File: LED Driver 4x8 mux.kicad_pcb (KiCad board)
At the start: 2 copper layers, 117 x 127.1 mm, 34 parts, among them J1 Barrel_Jack_Switch, J2 Conn_01x04_Female, J3 8P8C_Shielded_x4, M1 Fan_4pin, M2 Fan_4pin, M3 Fan_4pin, M4 Fan_4pin, Q1 SUM70060E, Q2 SUM70060E, Q3 SUM70060E, Q4 SUM70060E, Q5 DMN32D2LDF-7, Q6 DMN32D2LDF-7, U1 MIC4468ZWM-TR, U2 DC DC Converter

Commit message: update PCB
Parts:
- removed D1, D2, D3, D4: TVS_Diode, Custom Footprints:DO-214AA
- removed HS1, HS2: HS-PCB, Custom Footprints:Heatsink_910-40-2-23-2-B-0
- removed J2: Conn_01x04_Female, Custom Footprints:DC_DC_converter-3S4A_1218S1UP
- removed JP1, JP2, JP3, JP4, JP5: Quick Connect, Custom Footprints:4928TR-power
- removed M1, M2, M3, M4: Fan_4pin, Custom Footprints:4-pin_fan_SMD
- removed Q5, Q6: DMN32D2LDF-7, Package_TO_SOT_SMD:SOT-353_SC-70-5
- added C1: 22µF, Capacitor_SMD:C_1206_3216Metric, F.Cu at (227.6, 49.0)
- added C2: 2.2uF, Custom Footprints:0508_Capacitor, F.Cu at (243.7, 37.6)
- added C3: 22µF, Capacitor_SMD:C_1206_3216Metric, F.Cu at (236.1, 44.0)
- added C5: 2.2uF, Custom Footprints:0508_Capacitor, F.Cu at (252.3, 31.0)
- added U3: MIC4467YWM-TR, Custom Footprints:TC4468EOE, F.Cu at (218.4, 47.0)
- Q1, Q2, Q3, Q4: value SUM70060E -> IRF9358TRPBF-2x_p-channel; footprint Package_TO_SOT_SMD:TO-263-2 -> Custom Footprints:IRF9358TRPBF-2x_p-channel
- U1: value MIC4468ZWM-TR -> SN74LV138AT_D_16; footprint Custom Footprints:MIC4468ZWM-TR -> Custom Footprints:SN74LV138ATD
- U2: value DC DC Converter -> MIC4467YWM-TR; footprint Custom Footprints:Ref_only -> Custom Footprints:TC4468EOE
- moved U1 156.5 mm to (229.1, 34.8), turned to 0 degrees
- moved Q1 142.2 mm to (237.6, 32.3), turned to 0 degrees
- moved Q2 114.6 mm to (229.1, 44.0), turned to 0 degrees
- moved Q3 110.6 mm to (237.6, 39.0), turned to 0 degrees
- moved Q4 108.2 mm to (246.2, 32.3), turned to 0 degrees
- moved U2 42.1 mm to (218.4, 35.0)
- renumbered C1 to C4
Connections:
- C4 pad 2: /18V -> /+18V
- J1 pad 1: /12V -> /+18V
- J3 pad 1: Net-(J3-Pad1) -> /LED5+
- J3 pad 17: /CH1 -> /LED+
- J3 pad 18: GND -> /LED-
- J3 pad 19: /CH2 -> /LED+
- J3 pad 2: Net-(J3-Pad2) -> /LED-
- J3 pad 20: GND -> /LED-
- J3 pad 21: /CH3 -> /LED+
- J3 pad 22: GND -> /LED-
- J3 pad 23: /CH4 -> /LED+
- J3 pad 24: GND -> /LED-
- J3 pad 25: /Thermistor -> /LED1+
- J3 pad 26: /Therm1 -> /LED-
- J3 pad 27: /Thermistor -> /LED2+
- J3 pad 28: /Therm2 -> /LED-
- J3 pad 29: /Thermistor -> /LED3+
- J3 pad 3: /OUT2 -> /LED6+
- J3 pad 30: /Therm3 -> /LED-
- J3 pad 31: /Thermistor -> /LED4+
- J3 pad 32: /Therm4 -> /LED-
- J3 pad 4: GND -> /LED-
- J3 pad 5: /OUT3 -> /LED7+
- J3 pad 6: GND -> /LED-
- J3 pad 7: Net-(J3-Pad7) -> /LED8+
- J3 pad 8: Net-(J3-Pad8) -> /LED-
- J3 pad 9: /Fan_PWM -> /OUT1
- Q1 pad 1: /Gate4 -> /LED+
- Q1 pad 2: /LED4- -> /Gate1
- Q1 pad 3: /LED- -> /LED+
- Q2 pad 1: /Gate3 -> /LED+
- Q2 pad 2: /LED3- -> /Gate3
- Q2 pad 3: /LED- -> /LED+
- Q3 pad 1: /Gate2 -> /LED+
- Q3 pad 2: /LED2- -> /Gate5
- Q3 pad 3: /LED- -> /LED+
- Q4 pad 1: /Gate1 -> /LED+
- Q4 pad 2: /LED1- -> /Gate7
- Q4 pad 3: /LED- -> /LED+
- U1 pad 1: /CH4 -> /OUT1
- U1 pad 10: /CH1 -> /IN6
- U1 pad 11: /Gate1 -> /IN5
- U1 pad 12: /Gate2 -> /IN4
- U1 pad 13: /Gate3 -> /IN3
- U1 pad 14: /Gate4 -> /IN2
- U1 pad 15: /18V -> /IN1
- U1 pad 16: /18V -> /+5V
- U1 pad 2: /CH4 -> /OUT2
- U1 pad 3: /CH3 -> /OUT3
- U1 pad 4: /CH3 -> GND
- U1 pad 5: /CH2 -> GND
- U1 pad 6: /CH2 -> /+5V
- U1 pad 9: /CH1 -> /IN7
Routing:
- net /LED-: track 41.9 -> 244.9 mm, vias 0 -> 2
- net /OUT1: track 0.00 -> 198.6 mm
- net /Fan_PWM: track 198.6 -> 0.00 mm
- net GND: track 641.9 -> 498.1 mm, vias 109 -> 107
- net /LED+: track 59.0 -> 199.1 mm
- net /12V: track 134.8 -> 0.00 mm
- net /+18V: track 0.00 -> 134.8 mm
- net /Therm2: track 59.3 -> 0.00 mm
- net /CH1: track 56.8 -> 0.00 mm
- net /CH2: track 43.6 -> 0.00 mm
- net /CH3: track 39.8 -> 0.00 mm
- added copper zone on F.Cu, net /+18V
- removed copper zone on F.Cu, net /18V

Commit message: PCB draft finished
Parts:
- added PS1: PXO7805-500-M-TR, Custom Footprints:18V_to_5V_PXO7805-500-M-TR, F.Cu at (91.8, 131.8)
- Q1, Q2, Q3, Q4: value IRF9358TRPBF-2x_p-channel -> SO8_IRF9358TRPBF_INF
- moved C3 163.9 mm to (99.8, 135.0), turned to 90 degrees
- moved C2 162.3 mm to (107.7, 126.2)
- moved C1 157.8 mm to (88.7, 123.8)
- moved U1 156.3 mm to (107.3, 132.9)
- moved Q4 151.4 mm to (136.1, 136.2)
- moved C5 149.4 mm to (128.9, 115.2), turned to 270 degrees
- moved Q3 136.2 mm to (136.1, 129.8)
- moved Q1 132.2 mm to (136.1, 117.0)
- moved U3 129.6 mm to (121.4, 132.9)
- moved U2 128.9 mm to (121.7, 120.2)
- moved Q2 122.3 mm to (136.1, 123.4)
- moved H1 51.4 mm to (86.8, 97.4)
- moved H2 51.4 mm to (188.4, 97.4)
- moved LOGO1 44.6 mm to (168.4, 103.4), turned to 0 degrees
- moved LOGO3 41.1 mm to (169.6, 100.3), turned to 0 degrees
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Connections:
- J3 pad 1: /LED5+ -> /LED1+
- J3 pad 10: GND -> /LED-
- J3 pad 11: /OUT2 -> /LED6+
- J3 pad 12: GND -> /LED-
- J3 pad 13: /OUT3 -> /LED7+
- J3 pad 14: GND -> /LED-
- J3 pad 15: /Thermistor -> /LED8+
- J3 pad 16: GND -> /LED-
- J3 pad 25: /LED1+ -> /OUT1
- J3 pad 26: /LED- -> GND
- J3 pad 27: /LED2+ -> /OUT2
- J3 pad 28: /LED- -> GND
- J3 pad 29: /LED3+ -> /OUT3
- J3 pad 3: /LED6+ -> /LED2+
- J3 pad 30: /LED- -> GND
- J3 pad 31: /LED4+ -> /Thermistor
- J3 pad 32: /LED- -> GND
- J3 pad 5: /LED7+ -> /LED3+
- J3 pad 7: /LED8+ -> /LED4+
- J3 pad 9: /OUT1 -> /LED5+
- U1 pad 7: GND -> /IN8
- U3 pad 10: Net-(U3-Pad10) -> /IN8
- U3 pad 9: Net-(U3-Pad10) -> /IN8
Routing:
- net /LED+: track 199.1 -> 45.2 mm, vias 118 -> 0
- net /OUT1: track 198.6 -> 58.7 mm
- net GND: track 498.1 -> 382.6 mm, vias 107 -> 206
- net /Gate1: track 108.7 -> 8.01 mm
- net /Gate2: track 86.3 -> 7.49 mm
- net /LED2-: track 70.5 -> 0.00 mm
- net /LED3-: track 70.3 -> 0.00 mm
- net /LED4-: track 70.3 -> 0.00 mm
- net /Therm1: track 59.5 -> 0.00 mm
- net /Therm3: track 52.5 -> 0.00 mm
- net /Therm4: track 51.9 -> 0.00 mm
- net /Gate3: track 59.3 -> 8.21 mm
- net /LED1+: track 0.00 -> 48.1 mm
- net /LED2+: track 0.00 -> 44.4 mm
- net /LED-: track 244.9 -> 288.4 mm, vias 2 -> 0
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- removed copper zone on F.Cu, net /+18V
- removed copper zone on B.Cu, net /LED+
- removed copper zone on F.Cu, net /LED1-
- removed copper zone on F.Cu, net /LED2-
- removed copper zone on F.Cu, net /LED3-
- removed copper zone on F.Cu, net /LED4-
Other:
- board size 117 x 127.1 mm -> 117 x 72.4 mm
- board text added: "12-18V DC"
- board text added: "Designed by: Benjamin E. Smith Funded by: NIH P30EY003176 https://github.com/Llamero/High_speed_1x8_LED_mux"
- board text added: "High Speed 1:8 LED Mux"
- board text added: "LED Input 4 3 2 1"
- board text added: "LED Output 4 3 2 1"
- board text added: "LED Output 8 7 6 5"
- board text added: "Therm OUT3 OUT2 OUT1"
- board text removed: "*"
- board text removed: "+"
- board text removed: "+ - LED 1"
- board text removed: "+ - LED 2"
- board text removed: "+ - LED 3"
- board text removed: "+ - LED 4"
- board text removed: "-"
- board text removed: "12V"
- board text removed: "12V DC"
- board text removed: "18V"
- board text removed: "Channel Select 4 3 2 1"
- board text removed: "Designed by: Benjamin E. Smith Funded by: NIH P30EY003176 https://github.com/Llamero/High-current-4x1-LED-mux"
- board text removed: "GND"
- board text removed: "High Current 4:1 Mux"
- board text removed: "LED Fan"
- board text removed: "LED Input"
- board text removed: "LED Thermistor 4 3 2 1"
- board text removed: "N/C OUT3 OUT2 N/C"
- board text removed: "Therm OUT3 OUT2 Fan PWM"

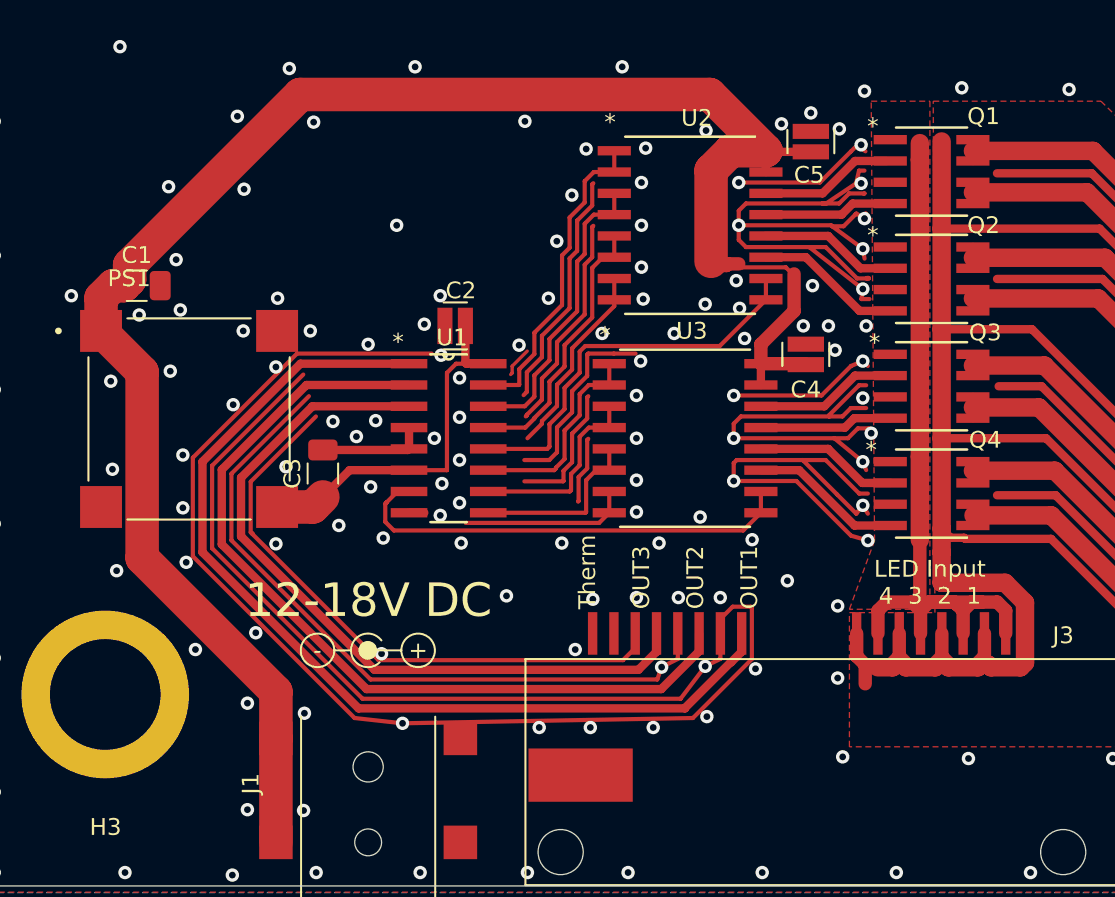
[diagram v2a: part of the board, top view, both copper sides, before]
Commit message: Add thermistor breakout
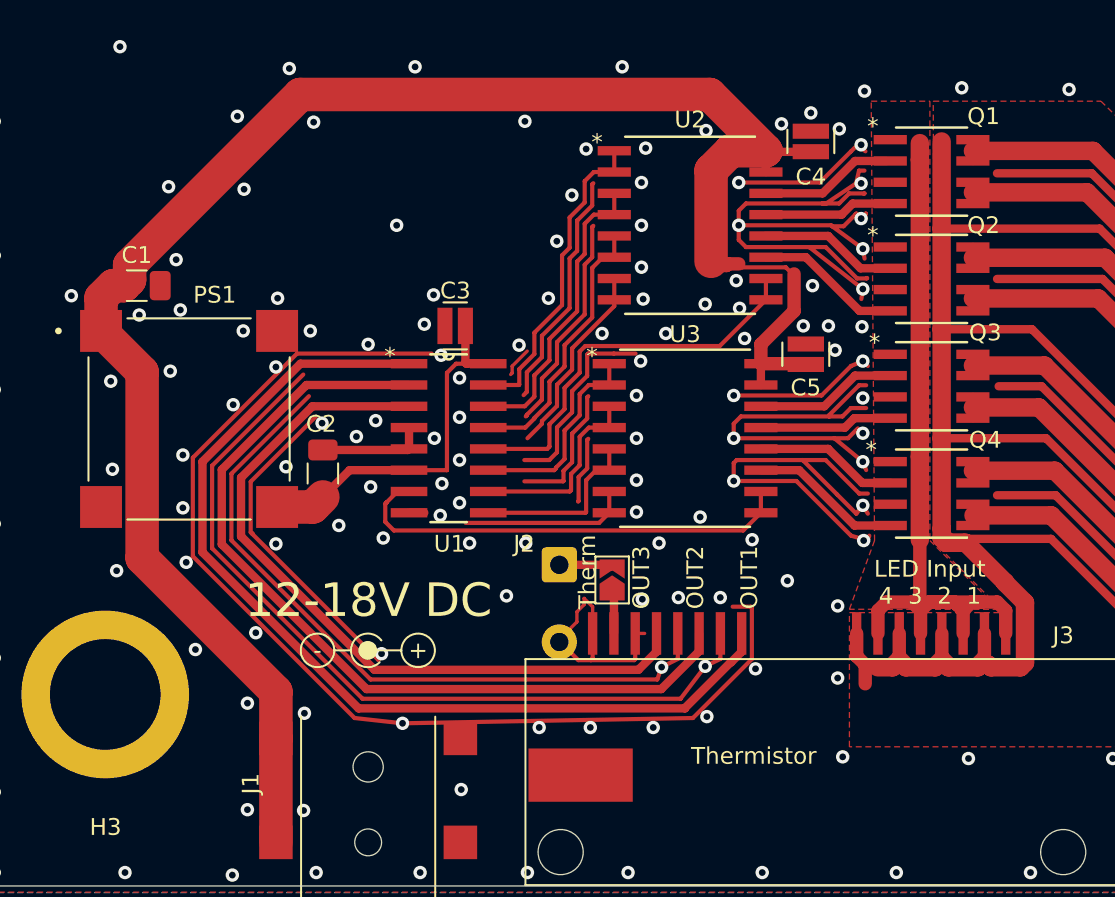
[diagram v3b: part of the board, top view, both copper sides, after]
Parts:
- added J2: Conn_01x02_Female, Connector_Wire:SolderWire-0.5sqmm_1x02_P4.6mm_D0.9mm_OD2.1mm, F.Cu at (113.9, 140.4)
- added JP1: Jumper_NO_Small, Jumper:SolderJumper-2_P1.3mm_Open_TrianglePad1.0x1.5mm, F.Cu at (117.0, 141.3)
- Q1, Q2, Q3, Q4: value SO8_IRF9358TRPBF_INF -> IRF9358TRPBF-2x_p-channel
- U2, U3: value MIC4467YWM-TR -> TC4468EOE
- moved C4 12.7 mm to (128.9, 115.2)
- moved C5 12.7 mm to (128.6, 127.9)
- renumbered C3 to C2, C2 to C3
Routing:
- net GND: track 382.6 -> 378.5 mm, vias 206 -> 205
- net /Thermistor: track 0.00 -> 3.60 mm
- net Net-(J2-Pad1): track 0.00 -> 3.15 mm
- net /LED-: track 288.4 -> 286.9 mm
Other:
- board text added: "Thermistor"

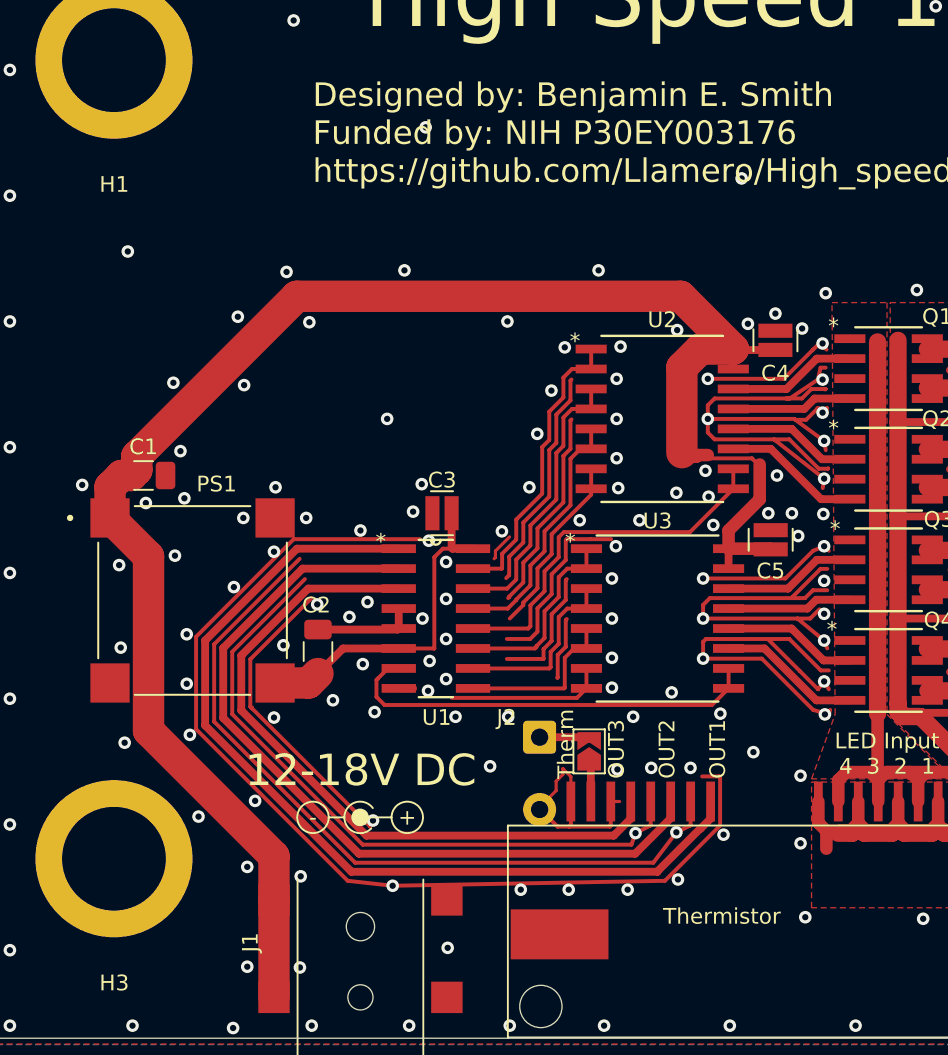
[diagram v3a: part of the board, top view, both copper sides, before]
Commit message: Capacitors positions optimized
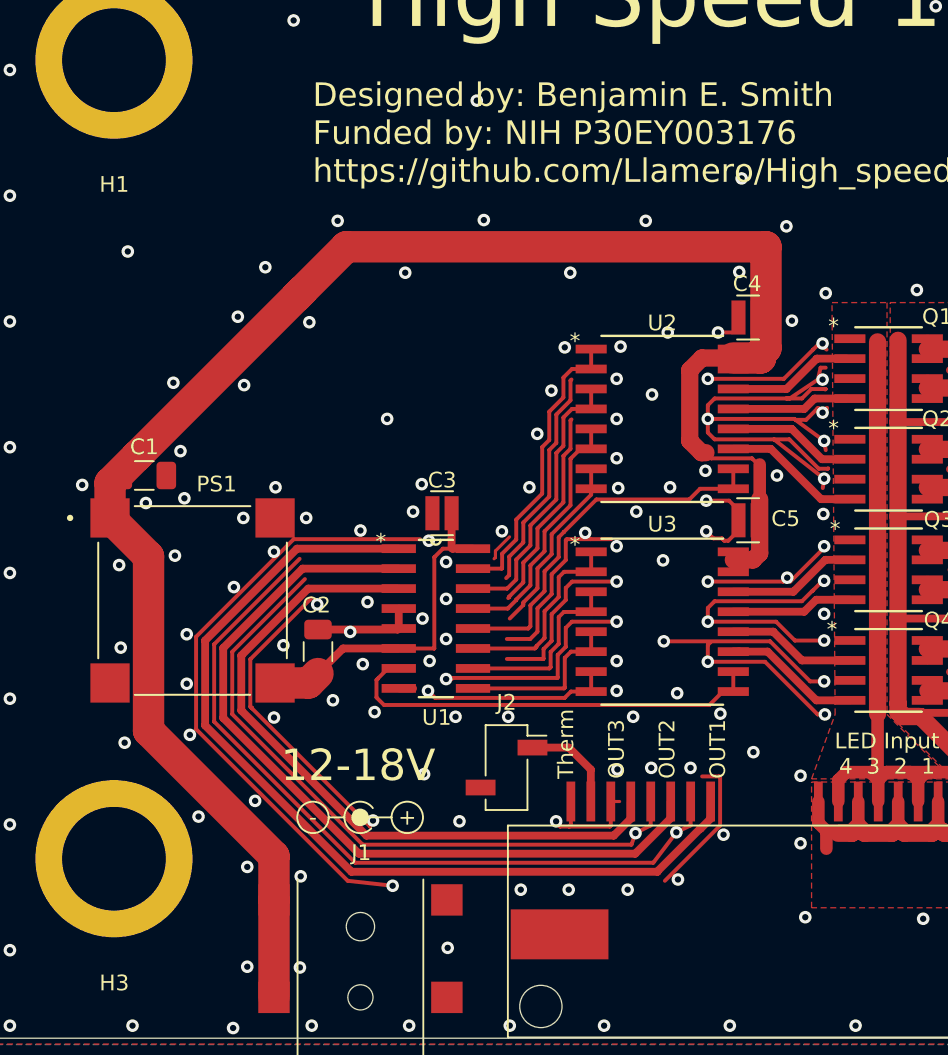
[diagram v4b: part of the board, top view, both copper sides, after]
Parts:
- removed JP1: Jumper_NO_Small, Jumper:SolderJumper-2_P1.3mm_Open_TrianglePad1.0x1.5mm
- J2: footprint Connector_Wire:SolderWire-0.5sqmm_1x02_P4.6mm_D0.9mm_OD2.1mm -> Connector_PinSocket_2.54mm:PinSocket_1x02_P2.54mm_Vertical_SMD_Pin1Right
- moved J2 2.86 mm to (111.8, 142.4), turned to 0 degrees
- moved C4 2.26 mm to (127.2, 113.8), turned to 0 degrees
- moved C5 1.90 mm to (127.2, 126.7), turned to 0 degrees
- moved U3 0.36 mm to (121.7, 133.1)
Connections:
- J2 pad 1: Net-(J2-Pad1) -> /Thermistor
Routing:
- net GND: track 378.5 -> 366.1 mm, vias 205 -> 211
- net /+18V: track 112.4 -> 116.3 mm
- net Net-(J2-Pad1): track 3.15 -> 0.00 mm
- net /Thermistor: track 3.60 -> 6.32 mm
- net /IN7: track 11.2 -> 12.2 mm
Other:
- board text added: "12-18V"
- board text removed: "12-18V DC"
- board text removed: "Thermistor"
